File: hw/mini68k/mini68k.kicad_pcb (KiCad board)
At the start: 2 copper layers, 27 parts, among them J1 Jack-DC, J2 FTDI header, SW1 SW_SPDT, SW2 SW_Push, U1 HM62256BLP-7, U2 68008D, U3 L7805, U4 28C256, U5 GAL16V8, U6 74LS05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

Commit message: initial layout
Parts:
- moved RN1 82.1 mm to (153.7, 86.4)
- moved J2 78.9 mm to (229.9, 108.0), turned to 180 degrees
- moved C2 2.84 mm to (139.7, 87.6)
- moved C11 2.54 mm to (189.2, 69.8), turned to 180 degrees
- moved C3 2.54 mm to (172.7, 69.8), turned to 180 degrees
- moved C5 2.54 mm to (215.9, 92.7), turned to 180 degrees
- moved C6 2.54 mm to (185.4, 108.0), turned to 180 degrees
- moved U4 1.27 mm to (144.8, 113.0)
- moved C8 1.27 mm to (153.7, 108.0), turned to 180 degrees
- turned JP1 to 270 degrees
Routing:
- net GND: track 0.00 -> 735.0 mm, vias 0 -> 8
- net VCC: track 0.00 -> 346.9 mm
- net CLK: track 0.00 -> 230.5 mm, vias 0 -> 1
- net DTACK: track 0.00 -> 168.8 mm, vias 0 -> 7
- net INTR: track 0.00 -> 160.6 mm, vias 0 -> 3
- net A9: track 0.00 -> 159.0 mm, vias 0 -> 1
- net DB6: track 0.00 -> 158.2 mm, vias 0 -> 4
- net A3: track 0.00 -> 157.4 mm, vias 0 -> 1
- net A1: track 0.00 -> 156.8 mm
- net R/W: track 0.00 -> 155.7 mm, vias 0 -> 3
- net A4: track 0.00 -> 146.8 mm, vias 0 -> 1
- net DB4: track 0.00 -> 145.2 mm, vias 0 -> 4
- net A15: track 0.00 -> 144.0 mm
- net A2: track 0.00 -> 143.4 mm
- net A8: track 0.00 -> 139.3 mm, vias 0 -> 2
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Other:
- net class Default: clearance 0.2 -> 0.254; trace_width 0.25 -> 0.254; via_dia 0.6 -> 1.016; via_drill 0.4 -> 0.508
- rule pad_to_mask_clearance: 0.2 -> 0
- rule trace_clearance: 0.2 -> 0.254
- rule trace_min: 0.2 -> 0.254
- rule via_min_drill: 0.3 -> 0.508
- rule via_min_size: 0.4 -> 1.016

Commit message: routing complete
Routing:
- net VCC: track 346.9 -> 498.8 mm, vias 0 -> 3
- net CLK: track 230.5 -> 229.0 mm
- net HALT: track 73.4 -> 74.4 mm

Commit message: 3d model
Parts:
- added REF**: MountingHole_3.2mm_M3, Mounting_Holes:MountingHole_3.2mm_M3, F.Cu at (228.6, 71.1)
- added REF**: MountingHole_3.2mm_M3, Mounting_Holes:MountingHole_3.2mm_M3, F.Cu at (229.9, 158.8)
- added REF**: MountingHole_3.2mm_M3, Mounting_Holes:MountingHole_3.2mm_M3, F.Cu at (95.2, 158.8)
- added REF**: MountingHole_3.2mm_M3, Mounting_Holes:MountingHole_3.2mm_M3, F.Cu at (96.5, 71.1)
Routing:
- added copper zone on B.Cu, net GND
- added copper zone on F.Cu, net VCC
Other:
- board outline added: 147.3 x 100.3 mm

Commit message: re-pour planes
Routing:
- net DB7: track 137.3 -> 133.7 mm
- net DB6: track 158.2 -> 156.6 mm
- net DB5: track 127.1 -> 126.3 mm
- added copper zone on F.Cu, net GND
- added copper zone on B.Cu, net VCC
- removed copper zone on B.Cu, net GND
- removed copper zone on F.Cu, net VCC
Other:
- board text added: "min68k John Roark 2018"

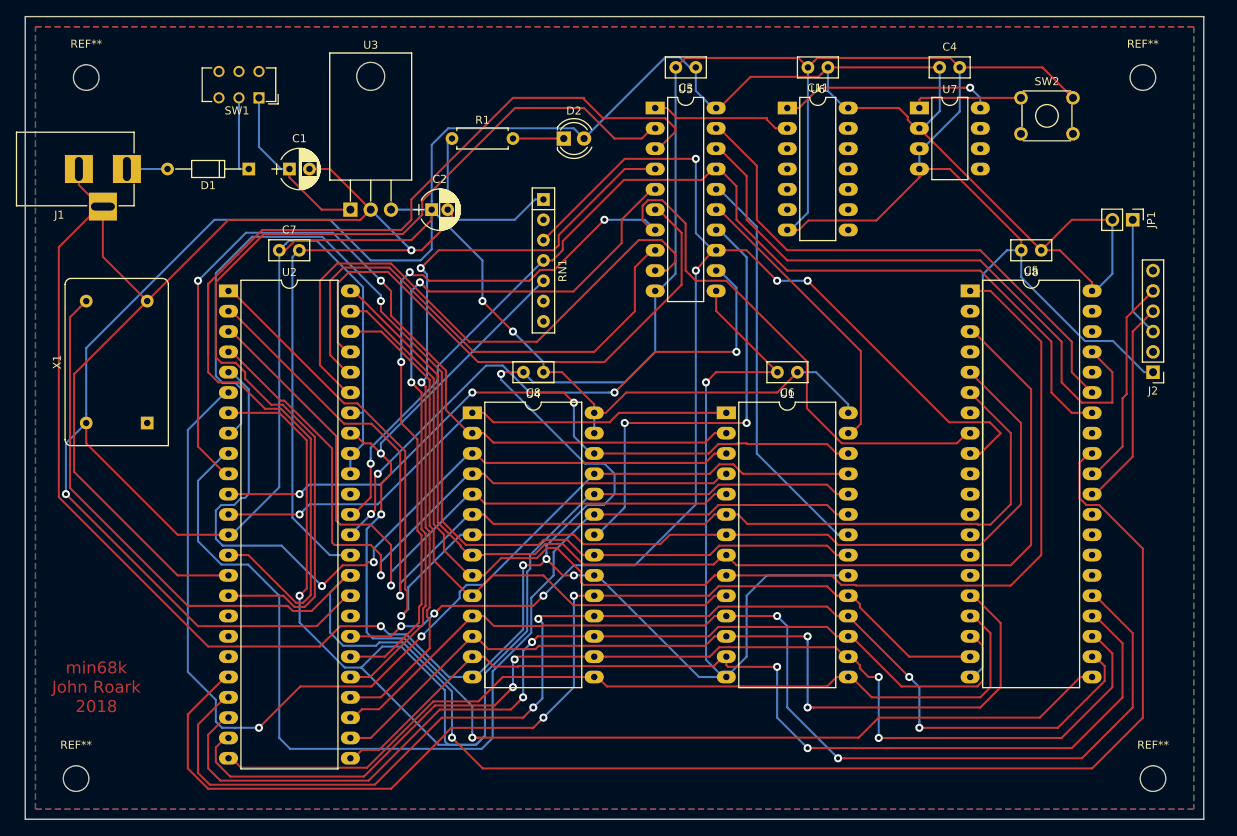
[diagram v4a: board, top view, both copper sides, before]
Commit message: v2 fixes:
  - swapped rx/tx
  - reset switch
  - pullup RST
  - pin one of X1
  - remove VCC plane from under 7805
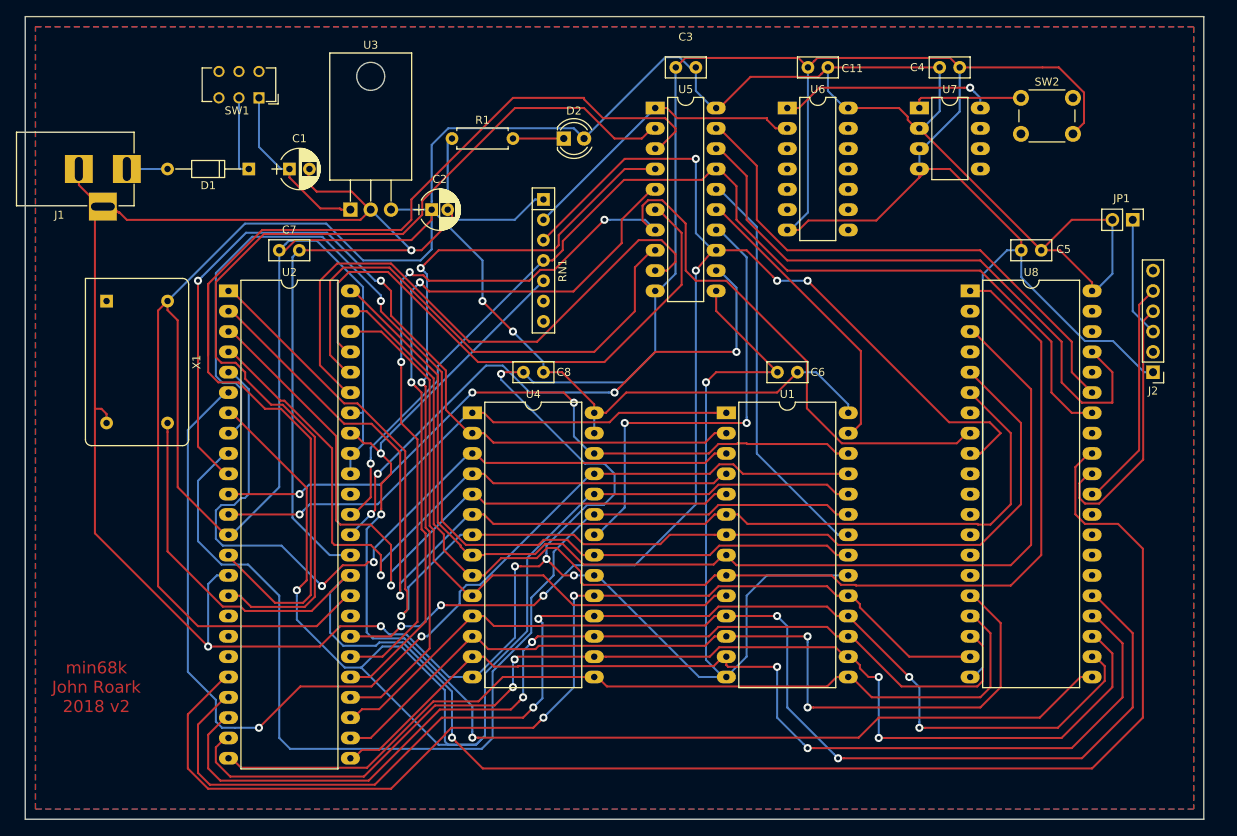
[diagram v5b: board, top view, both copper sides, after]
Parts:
- removed REF** (x4): MountingHole_3.2mm_M3, Mounting_Holes:MountingHole_3.2mm_M3
- SW2: footprint Buttons_Switches_THT:SW_TH_Tactile_Omron_B3F-10xx -> Buttons_Switches_THT:SW_PUSH_6mm
- moved X1 16.1 mm to (99.1, 99.1), turned to 270 degrees
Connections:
- J2 pad 2: Net-(J2-Pad2) -> (no net)
- J2 pad 4: TX1 -> RX1
- J2 pad 5: RX1 -> TX1
- J2 pad 6: Net-(J2-Pad6) -> (no net)
- RN1 pad 2: TR -> RST
- RN1 pad 6: Net-(RN1-Pad6) -> (no net)
- RN1 pad 7: Net-(RN1-Pad7) -> (no net)
- SW1 pad 3: Net-(SW1-Pad3) -> (no net)
- U2 pad 17: Net-(U2-Pad17) -> (no net)
- U2 pad 18: Net-(U2-Pad18) -> (no net)
- U2 pad 19: Net-(U2-Pad19) -> (no net)
- U2 pad 32: Net-(U2-Pad32) -> (no net)
- U2 pad 38: Net-(U2-Pad38) -> (no net)
- U6 pad 10: Net-(U6-Pad10) -> (no net)
- U6 pad 11: Net-(U6-Pad11) -> (no net)
- U6 pad 12: Net-(U6-Pad12) -> (no net)
- U6 pad 13: Net-(U6-Pad13) -> (no net)
- U6 pad 3: Net-(U6-Pad3) -> (no net)
- U6 pad 4: Net-(U6-Pad4) -> (no net)
- U6 pad 5: Net-(U6-Pad5) -> (no net)
- U6 pad 6: Net-(U6-Pad6) -> (no net)
- U6 pad 8: Net-(U6-Pad8) -> (no net)
- U6 pad 9: Net-(U6-Pad9) -> (no net)
- U7 pad 5: Net-(U7-Pad5) -> (no net)
- U7 pad 6: Net-(U7-Pad6) -> (no net)
- U7 pad 7: Net-(U7-Pad7) -> (no net)
- U8 pad 10: Net-(U8-Pad10) -> (no net)
- U8 pad 11: Net-(U8-Pad11) -> (no net)
- U8 pad 12: Net-(U8-Pad12) -> (no net)
- U8 pad 13: Net-(U8-Pad13) -> (no net)
- U8 pad 14: Net-(U8-Pad14) -> (no net)
- U8 pad 15: Net-(U8-Pad15) -> (no net)
- U8 pad 2: Net-(U8-Pad2) -> (no net)
- U8 pad 26: Net-(U8-Pad26) -> (no net)
- U8 pad 27: Net-(U8-Pad27) -> (no net)
- U8 pad 28: Net-(U8-Pad28) -> (no net)
- U8 pad 29: Net-(U8-Pad29) -> (no net)
- U8 pad 33: Net-(U8-Pad33) -> (no net)
- U8 pad 36: Net-(U8-Pad36) -> (no net)
- U8 pad 38: Net-(U8-Pad38) -> (no net)
- U8 pad 39: Net-(U8-Pad39) -> (no net)
- U8 pad 4: Net-(U8-Pad4) -> (no net)
- U8 pad 7: Net-(U8-Pad7) -> (no net)
- X1 pad 1: Net-(X1-Pad1) -> (no net)
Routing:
- net GND: track 734.6 -> 691.0 mm, vias 8 -> 9
- net CLK: track 229.0 -> 207.3 mm
- net RST: track 17.7 -> 37.4 mm
- net RX1: track 26.3 -> 33.5 mm
- net VCC: track 498.8 -> 493.9 mm, vias 3 -> 2
- net A9: track 159.0 -> 155.8 mm
- net TX1: track 26.3 -> 28.8 mm
- net R/W: track 155.7 -> 155.2 mm
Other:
- board text added: "min68k John Roark 2018 v2"
- board text removed: "min68k John Roark 2018"

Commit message: KiCad 5
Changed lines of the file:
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@@
-(kicad_pcb (version 4) (host pcbnew 4.0.7-e2-6376~61~ubuntu18.04.1)
+(kicad_pcb (version 20171130) (host pcbnew "(5.0.2-5-10.14)")
   (general
-    (links 148)
-    (no_connects 1)
-    (area 88.824999 63.424999 236.295001 163.905001)
     (thickness 1.6)
     (drawings 5)
@@
   )
   (layers
-    (0 F.Cu signal)
-    (31 B.Cu signal)
+    (0 F.Cu signal hide)
+    (31 B.Cu signal hide)
     (32 B.Adhes user)
     (33 F.Adhes user)
     (34 B.Paste user)
     (35 F.Paste user)
-    (36 B.SilkS user)
-    (37 F.SilkS user)
-    (38 B.Mask user)
-    (39 F.Mask user)
+    (36 B.SilkS user hide)
+    (37 F.SilkS user hide)
+    (38 B.Mask user hide)
+    (39 F.Mask user hide)
     (40 Dwgs.User user)
     (41 Cmts.User user)
@@
     (pad_drill 0.762)
     (pad_to_mask_clearance 0)
+    (solder_mask_min_width 0.25)
     (aux_axis_origin 96.52 71.12)
     (visible_elements FFFFFFFF)
@@
       (layerselection 0x00000_80000001)
       (usegerberextensions false)
+      (usegerberattributes false)
+      (usegerberadvancedattributes false)
+      (creategerberjobfile false)
       (excludeedgelayer true)
       (linewidth 0.100000)
@@
       (hpglpennumber 1)
       (hpglpenspeed 20)
-      (hpglpendiameter 15)
-      (hpglpenoverlay 2)
+      (hpglpendiameter 15.000000)
       (psnegative true)
       (psa4output false)
@@
       (drillshape 2)
       (scaleselection 1)
-      (outputdirectory postscript/))
+      (outputdirectory "postscript/"))
   )
   (net 0 "")
@@
     (descr "Through hole straight pin header, 1x02, 2.54mm pitch, single row")
     (tags "Through hole pin header THT 1x02 2.54mm single row")
-    (fp_text reference JP1 (at -2.667 1.397 360) (layer F.SilkS)
+    (fp_text reference JP1 (at -2.667 1.397) (layer F.SilkS)
       (effects (font (size 1 1) (thickness 0.15)))
     )
@@
     (fp_line (start 1.8 4.35) (end 1.8 -1.8) (layer F.CrtYd) (width 0.05))
     (fp_line (start 1.8 -1.8) (end -1.8 -1.8) (layer F.CrtYd) (width 0.05))
-    (fp_text user %R (at 0 1.27 360) (layer F.Fab)
+    (fp_text user %R (at 0 1.27) (layer F.Fab)
       (effects (font (size 1 1) (thickness 0.15)))
     )
@@
       (net 3 VCC))
     (model ${KISYS3DMOD}/TO_SOT_Packages_THT.3dshapes/TO-220-3_Horizontal.wrl
-      (at (xyz 0.1 0 0))
+      (offset (xyz 2.539999961853027 0 0))
       (scale (xyz 0.393701 0.393701 0.393701))
       (rotate (xyz 0 0 0))
@@
       (effects (font (size 1 1) (thickness 0.15)))
     )
-    (fp_text user %R (at 7.62 -3.81 360) (layer F.Fab)
+    (fp_text user %R (at 7.62 -3.81) (layer F.Fab)
       (effects (font (size 1 1) (thickness 0.15)))
     )
@@
       (net 13 MR))
     (model ${KISYS3DMOD}/Buttons_Switches_THT.3dshapes/SW_PUSH_6mm.wrl
-      (at (xyz 0.005 0 0))
+      (offset (xyz 0.1269999980926514 0 0))
       (scale (xyz 0.3937 0.3937 0.3937))
       (rotate (xyz 0 0 0))
@@
   (segment (start 228.766 107.95) (end 224.86701 104.05101) (width 0.254) (layer B.Cu) (net 2))
   (segment (start 224.86701 104.05101) (end 221.36081 104.05101) (width 0.254) (layer B.Cu) (net 2))
-  (segment (start 213.4 92.71) (end 211.612118 92.71) (width 0.254) (layer B.Cu) (net 2))
-  (segment (start 211.612118 92.71) (end 208.59101 95.731108) (width 0.254) (layer B.Cu) (net 2))
   (segment (start 182.92 107.95) (end 175.26 107.95) (width 0.254) (layer F.Cu) (net 2))
   (segment (start 175.26 107.95) (end 173.99 109.22) (width 0.254) (layer F.Cu) (net 2))
-  (segment (start 208.59101 95.731108) (end 208.59101 144.86899) (width 0.254) (layer B.Cu) (net 2))
-  (segment (start 208.59101 144.86899) (end 207.41 146.05) (width 0.254) (layer B.Cu) (net 2))
-  (segment (start 207.41 146.05) (end 207.01 146.05) (width 0.254) (layer B.Cu) (net 2))
   (via (at 144.78 146.05) (size 1.016) (drill 0.508) (layers F.Cu B.Cu) (net 2))
   (segment (start 173.99 109.22) (end 173.99 143.91) (width 0.254) (layer B.Cu) (net 2))
@@
   (segment (start 174.078999 109.131001) (end 173.99 109.22) (width 0.254) (layer F.Cu) (net 2))
   (via (at 173.99 109.22) (size 1.016) (drill 0.508) (layers F.Cu B.Cu) (net 2))
+  (segment (start 210.82 93.502118) (end 210.82 142.64) (width 0.254) (layer B.Cu) (net 2))
+  (segment (start 211.612118 92.71) (end 210.82 93.502118) (width 0.254) (layer B.Cu) (net 2))
+  (segment (start 207.41 146.05) (end 207.01 146.05) (width 0.254) (layer B.Cu) (net 2))
+  (segment (start 210.82 142.64) (end 207.41 146.05) (width 0.254) (layer B.Cu) (net 2))
+  (segment (start 213.4 92.71) (end 211.612118 92.71) (width 0.254) (layer B.Cu) (net 2))
   (segment (start 106.68 99.06) (end 105.498999 100.241001) (width 0.254) (layer F.Cu) (net 3))
   (segment (start 105.498999 100.241001) (end 105.498999 134.708999) (width 0.254) (layer F.Cu) (net 3))
@@
     (connect_pads (clearance 0.508))
     (min_thickness 0.254)
-    (fill yes (arc_segments 16) (thermal_gap 0.508) (thermal_bridge_width 0.508))
+    (fill (arc_segments 16) (thermal_gap 0.508) (thermal_bridge_width 0.508))
     (polygon
       (pts
@@
     (connect_pads (clearance 0.508))
     (min_thickness 0.254)
-    (fill yes (arc_segments 16) (thermal_gap 0.508) (thermal_bridge_width 0.508))
+    (fill (arc_segments 16) (thermal_gap 0.508) (thermal_bridge_width 0.508))
     (polygon
       (pts

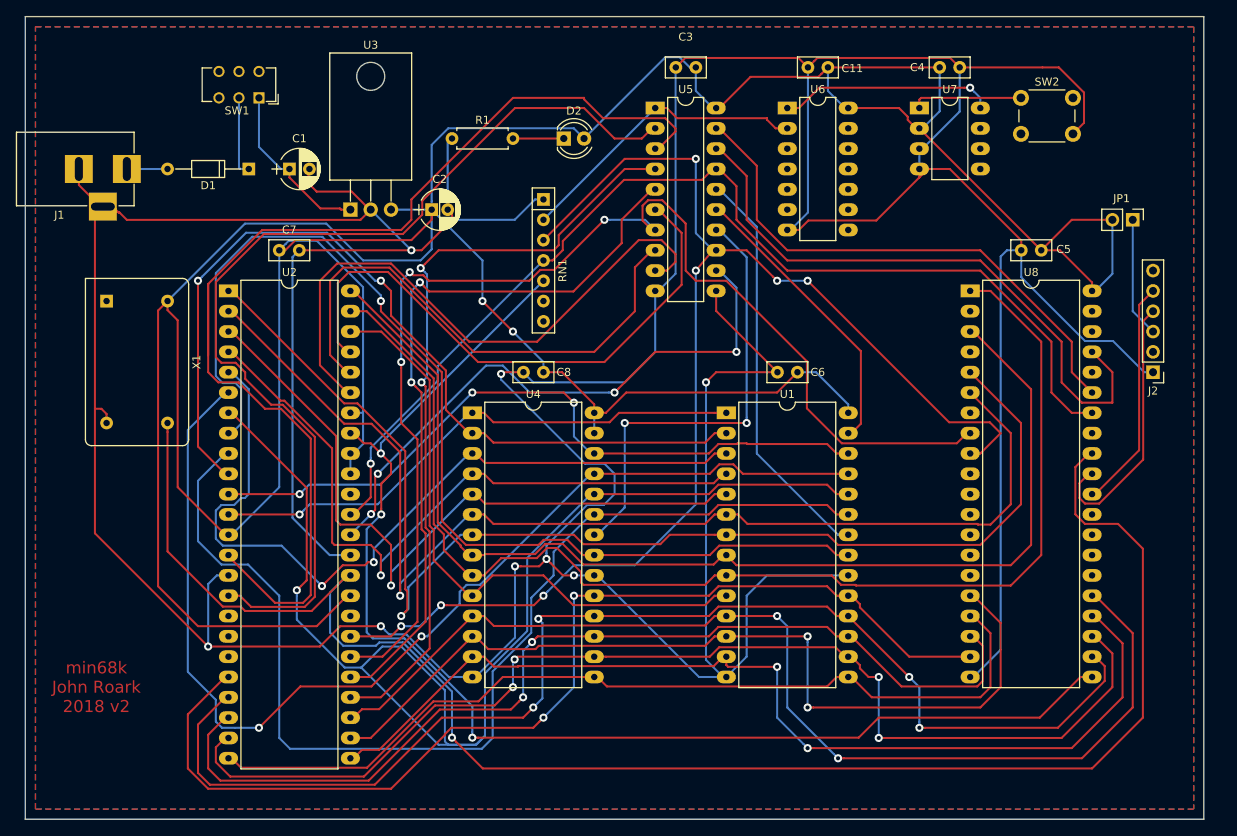
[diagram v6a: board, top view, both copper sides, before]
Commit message: update footprints, expose i/o from 68681
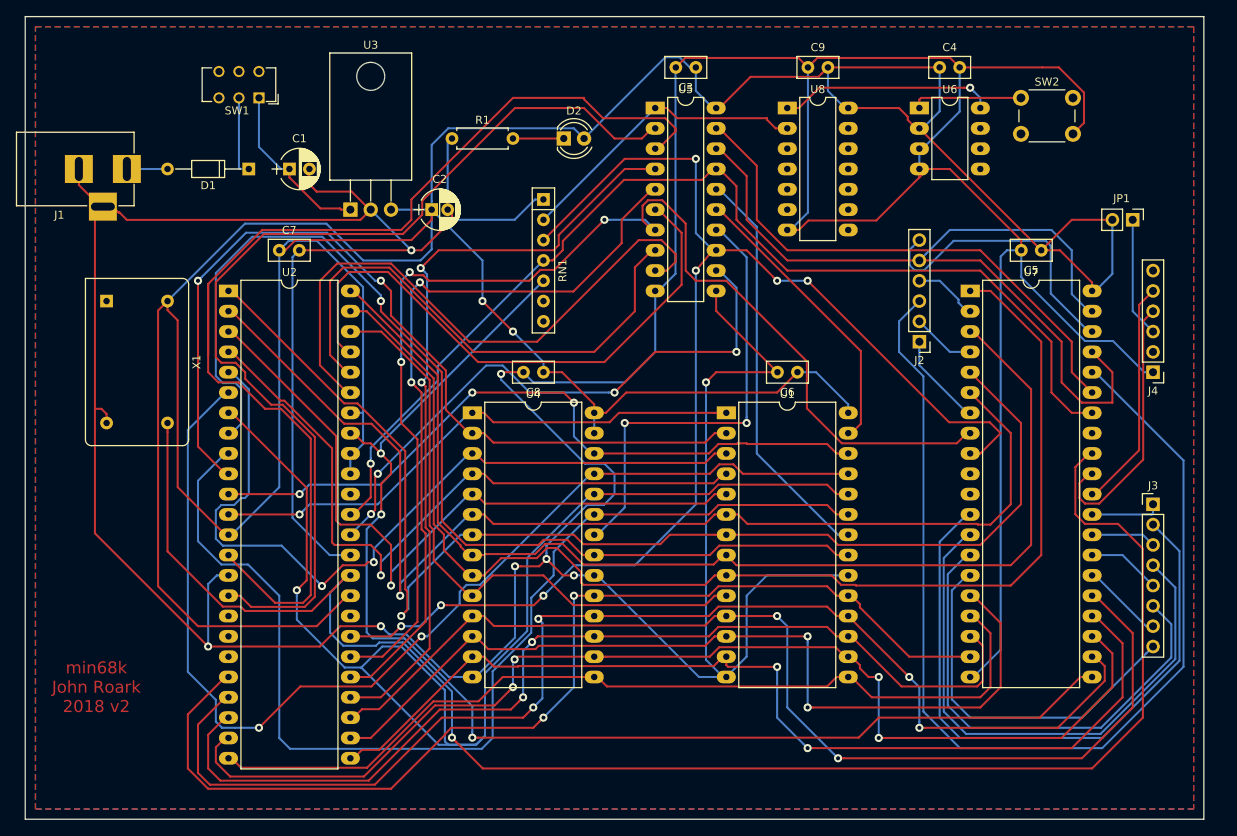
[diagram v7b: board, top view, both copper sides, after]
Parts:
- removed C11: .1u, Capacitors_THT:C_Disc_D5.0mm_W2.5mm_P2.50mm
- added C9: .1u, Capacitor_THT:C_Disc_D5.0mm_W2.5mm_P2.50mm, F.Cu at (186.7, 69.8)
- added J3: 8-bit output port, Connector_PinHeader_2.54mm:PinHeader_1x08_P2.54mm_Vertical, F.Cu at (229.9, 124.5)
- added J4: FTDI header, Connector_PinHeader_2.54mm:PinHeader_1x06_P2.54mm_Vertical, F.Cu at (229.9, 108.0)
- C3, C4, C5, C6, C7, C8: footprint Capacitors_THT:C_Disc_D5.0mm_W2.5mm_P2.50mm -> Capacitor_THT:C_Disc_D5.0mm_W2.5mm_P2.50mm
- J2: value FTDI header -> 6-bit input port; footprint Pin_Headers:Pin_Header_Straight_1x06_Pitch2.54mm -> Connector_PinHeader_2.54mm:PinHeader_1x06_P2.54mm_Vertical
- U1, U4: footprint Housings_DIP:DIP-28_W15.24mm_LongPads -> Package_DIP:DIP-28_W15.24mm_LongPads
- U2: footprint Housings_DIP:DIP-48_W15.24mm_LongPads -> Package_DIP:DIP-48_W15.24mm_LongPads
- U5: footprint Housings_DIP:DIP-20_W7.62mm_LongPads -> Package_DIP:DIP-20_W7.62mm_LongPads
- U6: value 74LS05 -> MAX708CPA+; footprint Housings_DIP:DIP-14_W7.62mm_LongPads -> Package_DIP:DIP-8_W7.62mm_LongPads
- U7: value MAX708CPA+ -> 68681; footprint Housings_DIP:DIP-8_W7.62mm_LongPads -> Package_DIP:DIP-40_W15.24mm_LongPads
- U8: value 68681 -> 74LS05; footprint Housings_DIP:DIP-40_W15.24mm_LongPads -> Package_DIP:DIP-14_W7.62mm_LongPads
- moved U8 32.3 mm to (184.2, 74.9)
- moved J2 29.5 mm to (200.7, 104.1)
- moved U7 23.7 mm to (207.0, 97.8)
- moved U6 16.5 mm to (200.7, 74.9)
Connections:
- J2 pad 1: GND -> IP0
- J2 pad 2: (no net) -> IP1
- J2 pad 3: Net-(J2-Pad3) -> IP2
- J2 pad 4: RX1 -> IP3
- J2 pad 5: TX1 -> IP4
- J2 pad 6: (no net) -> IP5
- JP1 pad 1: Net-(J2-Pad3) -> Net-(J4-Pad3)
- RN1 pad 6: (no net) -> Net-(RN1-Pad6)
- RN1 pad 7: (no net) -> Net-(RN1-Pad7)
- SW1 pad 3: (no net) -> Net-(SW1-Pad3)
- U2 pad 17: (no net) -> Net-(U2-Pad17)
- U2 pad 18: (no net) -> Net-(U2-Pad18)
- U2 pad 19: (no net) -> Net-(U2-Pad19)
- U2 pad 32: (no net) -> Net-(U2-Pad32)
- U2 pad 38: (no net) -> Net-(U2-Pad38)
- U6 pad 1: Net-(U6-Pad1) -> MR
- U6 pad 2: RST -> VCC
- U6 pad 3: (no net) -> GND
- U6 pad 4: (no net) -> GND
- U6 pad 5: (no net) -> Net-(U6-Pad5)
- U6 pad 6: (no net) -> Net-(U6-Pad6)
- U6 pad 7: GND -> Net-(U6-Pad7)
- U6 pad 8: (no net) -> Net-(U6-Pad8)
- U7 pad 1: MR -> A1
- U7 pad 2: VCC -> IP3
- U7 pad 3: GND -> A2
- U7 pad 4: GND -> IP1
- U7 pad 5: (no net) -> A3
- U7 pad 6: (no net) -> A4
- U7 pad 7: (no net) -> IP0
- U7 pad 8: Net-(U6-Pad1) -> R/W
- U8 pad 1: A1 -> Net-(U6-Pad8)
- U8 pad 10: (no net) -> Net-(U8-Pad10)
- U8 pad 11: (no net) -> Net-(U8-Pad11)
- U8 pad 12: (no net) -> Net-(U8-Pad12)
- U8 pad 13: (no net) -> Net-(U8-Pad13)
- U8 pad 14: (no net) -> VCC
- U8 pad 2: (no net) -> RST
- U8 pad 3: A2 -> Net-(U8-Pad3)
- U8 pad 4: (no net) -> Net-(U8-Pad4)
- U8 pad 5: A3 -> Net-(U8-Pad5)
- U8 pad 6: A4 -> Net-(U8-Pad6)
- U8 pad 7: (no net) -> GND
- U8 pad 8: R/W -> Net-(U8-Pad8)
- U8 pad 9: DTACK -> Net-(U8-Pad9)
- X1 pad 1: (no net) -> Net-(X1-Pad1)
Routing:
- net IP2: track 0.00 -> 134.0 mm
- net OP1: track 0.00 -> 80.6 mm
- net OP3: track 0.00 -> 70.6 mm
- net OP5: track 0.00 -> 60.3 mm
- net OP7: track 0.00 -> 46.5 mm
- net IP5: track 0.00 -> 36.4 mm
- net IP4: track 0.00 -> 30.6 mm
- net Net-(U6-Pad8): track 0.00 -> 27.0 mm, vias 0 -> 1
- net Net-(U6-Pad1): track 27.0 -> 0.00 mm, vias 1 -> 0
- net Net-(J4-Pad3): track 0.00 -> 15.0 mm
- net Net-(J2-Pad3): track 15.0 -> 0.00 mm
- net IP0: track 0.00 -> 11.8 mm
- net OP6: track 0.00 -> 10.3 mm
- net OP4: track 0.00 -> 9.20 mm
- net OP0: track 0.00 -> 8.79 mm
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
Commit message: run drc and fix issues
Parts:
- moved C9 2.50 mm to (189.2, 69.8), turned to 180 degrees
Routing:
- net MR: track 13.8 -> 20.3 mm
- net GND: track 691.0 -> 697.5 mm
- net UART_CS: track 66.9 -> 68.8 mm
